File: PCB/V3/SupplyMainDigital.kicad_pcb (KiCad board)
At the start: 2 copper layers, 64 x 48 mm, 94 parts, among them J1 IN, J2 3.3V, J3 OUT, J4 Conn_01x01, J5 Conn_01x01, J6 Conn_01x01, J7 Conn_01x01, P1 LEDs, P5 PGM, P6 SERIAL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

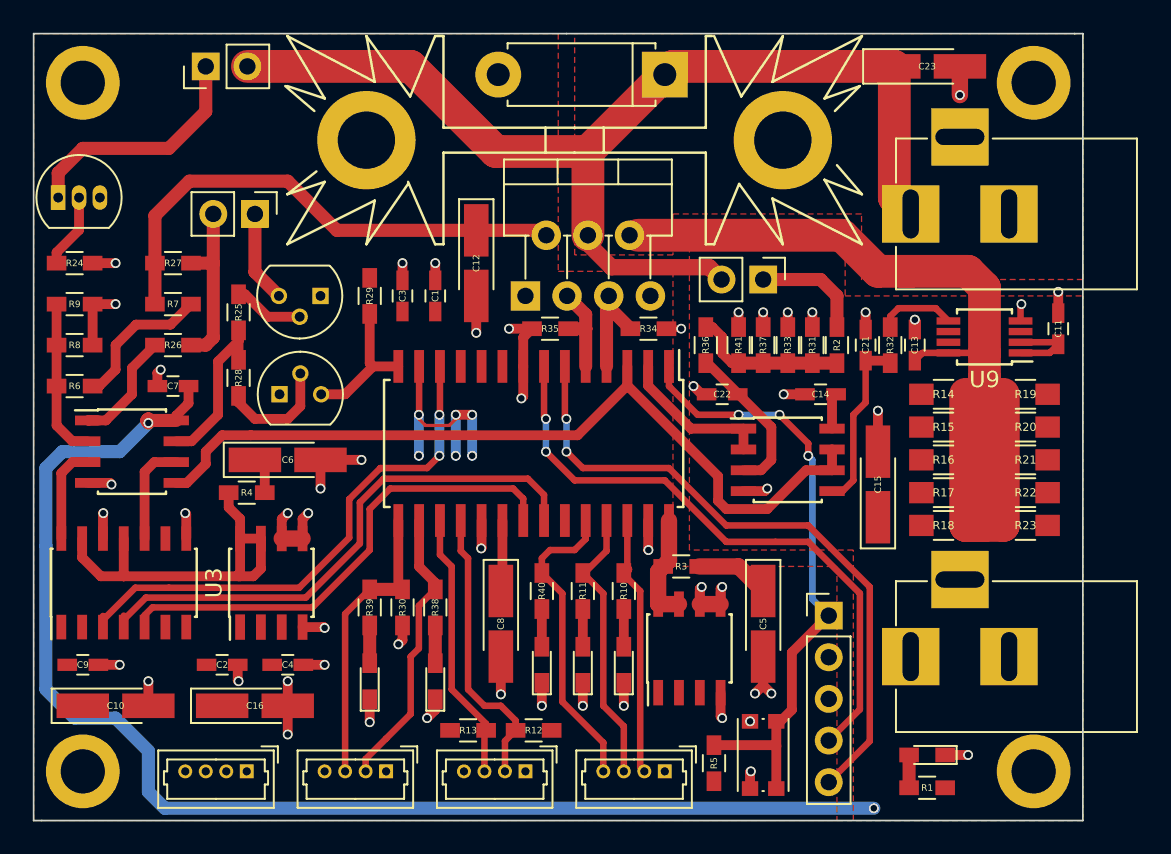
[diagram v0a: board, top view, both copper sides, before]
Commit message: first application + uart api
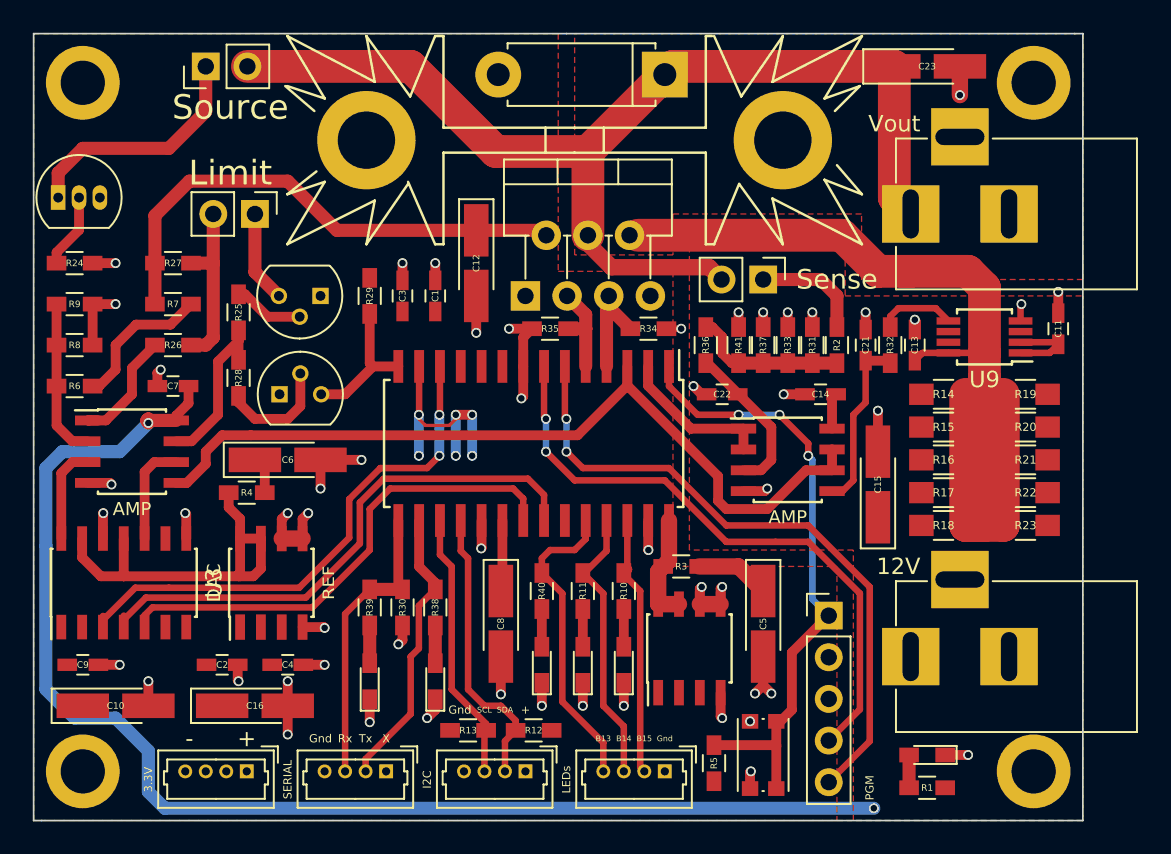
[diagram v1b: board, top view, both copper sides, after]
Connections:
- J4 pad 1: Net-(J4-Pad1) -> (no net)
- J5 pad 1: Net-(J5-Pad1) -> (no net)
- J6 pad 1: Net-(J6-Pad1) -> (no net)
- J7 pad 1: Net-(J7-Pad1) -> (no net)
- P6 pad 1: +3V3 -> (no net)
- U2 pad 2: Net-(U2-Pad2) -> (no net)
- U3 pad 2: Net-(U3-Pad2) -> (no net)
- U4 pad 2: Net-(U4-Pad2) -> (no net)
- U4 pad 6: Net-(U4-Pad6) -> (no net)
- U4 pad 7: Net-(U4-Pad7) -> (no net)
- U5 pad 10: Net-(U5-Pad10) -> (no net)
- U5 pad 11: Net-(U5-Pad11) -> (no net)
- U5 pad 23: /SPI_SDI -> (no net)
- U5 pad 9: Net-(U5-Pad9) -> (no net)
- U6 pad 1: Net-(U6-Pad1) -> (no net)
- U6 pad 7: Net-(U6-Pad7) -> (no net)
- U9 pad 3: Net-(U9-Pad3) -> (no net)
- U9 pad 6: Net-(U9-Pad6) -> (no net)
- U9 pad 7: Net-(U9-Pad7) -> (no net)
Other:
- board text added: "+"
- board text added: "-"
- board text added: "12V"
- board text added: "AMP"
- board text added: "B13"
- board text added: "B14"
- board text added: "B15"
- board text added: "DAC"
- board text added: "Gnd"
- board text added: "Limit"
- board text added: "REF"
- board text added: "Rx"
- board text added: "SCL"
- board text added: "SDA"
- board text added: "Sense"
- board text added: "Source"
- board text added: "Tx"
- board text added: "Vout"
- board text added: "X"
